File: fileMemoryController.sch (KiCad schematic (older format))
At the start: 13 parts, among them U10 74LVC1G74, U12 74AHC244, U15 74AHCT1G04, U21 74AHCT244, U22 74CBTLV16212, U40 74AHC273, U41 74AHC1G04

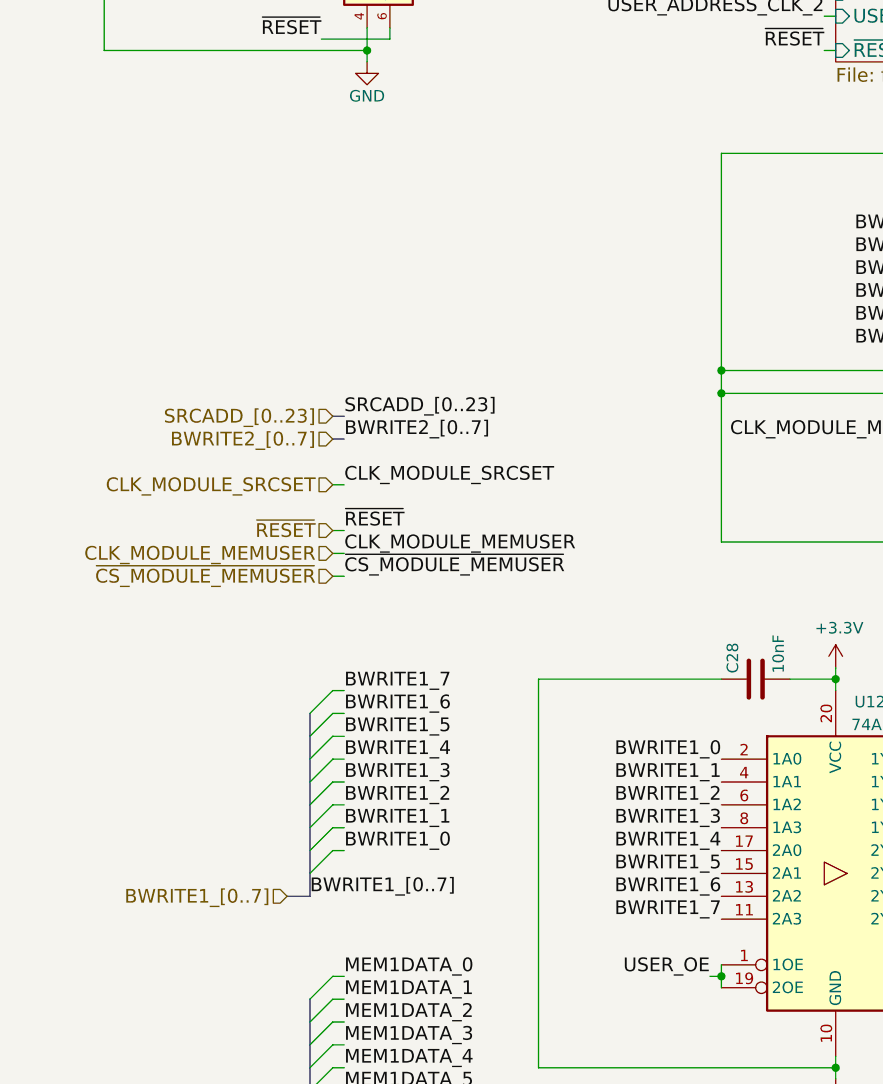
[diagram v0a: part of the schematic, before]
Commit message: V5.1 (#15)
* Remove compatibility for 5.0, 4.x and add 5.1+

* Fix switched pins on SN74LV393A #7

* Removed capacitor on 12V #11

* Add/Modify power decoupling capacitor #10

* Removing ADDSCR_CLK delay #9

* Schematics : set version 5.1, 2021 copyright and publish date

* Put non-electrolytic capacitor #10

* Set every capacitor size to 0805

* Add new footprint for J7 TE_3-641124-6 #6

* Schematic : set pinHeader on J12 #4

* Netlist, apply change to board, clean track, #6 #4 #12 #10

* Set version to 5.1, 2021 copyright and date, replace the missing QRcode

* Back the MM1 connectors #8

* Replace capacitor for U22 U23 U24 #13

* Better decoupling

* Increase version, year to 2021, clear status

* Precise the molex connector for power supply

* First step, import ses

* Clean bottom layer

* #14 Set the BWRITE2 bus instead of BWRITE1 on U12

* netlist, redo autorouting and cleaning

* use shields.io for colored badge

* Update gerbert files

* Changelog, updated BOM

* Small revision on blockDiagram

* Update README.md

* exporting pcb in pdf

* 3D images, diagram.png

* Update schematics pdf

* redo wavedrom_24bitsCounter
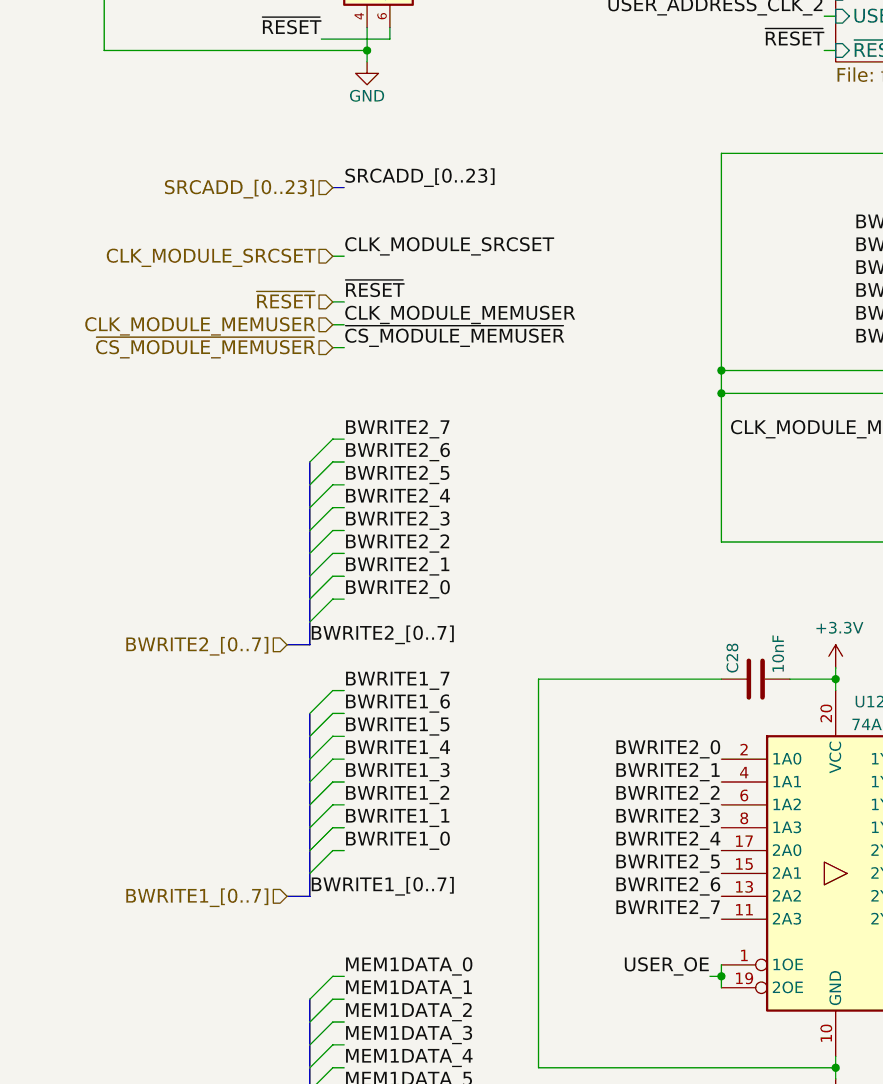
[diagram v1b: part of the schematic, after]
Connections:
- net BWRITE1_0: no longer U12.2 (1A0)
- net BWRITE1_1: no longer U12.4 (1A1)
- net BWRITE1_2: no longer U12.6 (1A2)
- net BWRITE1_3: no longer U12.8 (1A3)
- net BWRITE1_4: no longer U12.17 (2A0)
- net BWRITE1_5: no longer U12.15 (2A1)
- net BWRITE1_6: no longer U12.13 (2A2)
- net BWRITE1_7: no longer U12.11 (2A3)
- new net BWRITE2_0: U12.2 (1A0)
- new net BWRITE2_1: U12.4 (1A1)
- new net BWRITE2_2: U12.6 (1A2)
- new net BWRITE2_3: U12.8 (1A3)
- new net BWRITE2_4: U12.17 (2A0)
- new net BWRITE2_5: U12.15 (2A1)
- new net BWRITE2_6: U12.13 (2A2)
- new net BWRITE2_7: U12.11 (2A3)
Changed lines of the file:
@@
 Sheet 8 10
 Title "GCM"
-Date "2020-11-23"
-Rev "V5.0"
+Date "2021-02-16"
+Rev "V5.1"
 Comp "Guillaume Guillet"
-Comment1 "Copyright Guillaume Guillet 2020"
+Comment1 "Copyright Guillaume Guillet 2021"
 Comment2 "Licensed under CERN-OHL-W v2 or later"
 Comment3 ""
@@
 	0    -1   -1   0
 $EndComp
-Text Label 3300 4600 2    60   ~ 0
-BWRITE1_0
-Text Label 3300 4700 2    60   ~ 0
-BWRITE1_1
-Text Label 3300 4800 2    60   ~ 0
-BWRITE1_2
-Text Label 3300 4900 2    60   ~ 0
-BWRITE1_3
-Text Label 3300 5000 2    60   ~ 0
-BWRITE1_4
-Text Label 3300 5100 2    60   ~ 0
-BWRITE1_5
-Text Label 3300 5200 2    60   ~ 0
-BWRITE1_6
-Text Label 3300 5300 2    60   ~ 0
-BWRITE1_7
 Wire Wire Line
 	3800 6000 3800 5950
@@
 Text Label 1650 7400 0    60   ~ 0
 MEM2DATA_7
-Text Label 1650 3400 0    60   ~ 0
+Text Label 1650 2400 0    60   ~ 0
 CLK_MODULE_SRCSET
 Text Label 10250 1200 2    60   ~ 0
@@
 	1    0    0    -1
 $EndComp
-Text HLabel 1600 3200 0    60   Input ~ 0
-BWRITE2_[0..7]
-Text HLabel 1600 3100 0    60   Input ~ 0
+Text HLabel 1600 2100 0    60   Input ~ 0
 SRCADD_[0..23]
-Text Label 1650 3100 0    60   ~ 0
+Text Label 1650 2100 0    60   ~ 0
 SRCADD_[0..23]
-Text Label 1650 3200 0    60   ~ 0
-BWRITE2_[0..7]
-Wire Bus Line
-	1600 3100 1650 3100
-Wire Bus Line
-	1650 3200 1600 3200
+Wire Bus Line
+	1600 2100 1650 2100
 Text Label 3750 850  2    60   ~ 0
 SRCADD_[0..23]
@@
 Wire Wire Line
 	10050 6350 10100 6350
-Text HLabel 1600 3400 0    60   Input ~ 0
+Text HLabel 1600 2400 0    60   Input ~ 0
 CLK_MODULE_SRCSET
 Wire Wire Line
-	1600 3400 1650 3400
+	1600 2400 1650 2400
 Wire Wire Line
 	7850 3900 7150 3900
@@
 Text Label 4350 2800 2    60   ~ 0
 BWRITE1_5
-Text Label 1650 3700 0    60   ~ 0
+Text Label 1650 2700 0    60   ~ 0
 CLK_MODULE_MEMUSER
-Text HLabel 1600 3700 0    60   Input ~ 0
+Text HLabel 1600 2700 0    60   Input ~ 0
 CLK_MODULE_MEMUSER
 Wire Wire Line
-	1600 3700 1650 3700
-Text Label 1650 3600 0    60   ~ 0
+	1600 2700 1650 2700
+Text Label 1650 2600 0    60   ~ 0
 ~RESET
-Text HLabel 1600 3600 0    60   Input ~ 0
+Text HLabel 1600 2600 0    60   Input ~ 0
 ~RESET
 Wire Wire Line
-	1600 3600 1650 3600
+	1600 2600 1650 2600
 Text Label 1550 1450 2    60   ~ 0
 ~RESET
@@
 Text Label 5350 2500 0    60   ~ 0
 USER_~OE
-Text Label 1650 3800 0    60   ~ 0
+Text Label 1650 2800 0    60   ~ 0
 ~CS_MODULE_MEMUSER
-Text HLabel 1600 3800 0    60   Input ~ 0
+Text HLabel 1600 2800 0    60   Input ~ 0
 ~CS_MODULE_MEMUSER
 Wire Wire Line
-	1600 3800 1650 3800
+	1600 2800 1650 2800
 Text Label 7750 6000 2    60   ~ 0
 USER_~OE
@@
 	7150 3900 7150 4300
 Connection ~ 7150 3900
+Text HLabel 1400 4100 0    60   Input ~ 0
+BWRITE2_[0..7]
+Wire Bus Line
+	1500 4100 1400 4100
+Wire Wire Line
+	1650 3900 1600 3900
+Wire Wire Line
+	1650 3800 1600 3800
+Wire Wire Line
+	1650 3700 1600 3700
+Wire Wire Line
+	1650 3600 1600 3600
+Wire Wire Line
+	1650 3500 1600 3500
+Wire Wire Line
+	1650 3400 1600 3400
+Wire Wire Line
+	1650 3300 1600 3300
+Wire Wire Line
+	1650 3200 1600 3200
+Entry Wire Line
+	1600 3900 1500 4000
+Entry Wire Line
+	1600 3800 1500 3900
+Entry Wire Line
+	1600 3700 1500 3800
+Entry Wire Line
+	1600 3600 1500 3700
+Entry Wire Line
+	1600 3500 1500 3600
+Entry Wire Line
+	1600 3400 1500 3500
+Entry Wire Line
+	1600 3300 1500 3400
+Entry Wire Line
+	1600 3200 1500 3300
+Text Label 1500 4100 0    60   ~ 0
+BWRITE2_[0..7]
+Text Label 1650 3900 0    60   ~ 0
+BWRITE2_0
+Text Label 1650 3800 0    60   ~ 0
+BWRITE2_1
+Text Label 1650 3700 0    60   ~ 0
+BWRITE2_2
+Text Label 1650 3600 0    60   ~ 0
+BWRITE2_3
+Text Label 1650 3500 0    60   ~ 0
+BWRITE2_4
+Text Label 1650 3400 0    60   ~ 0
+BWRITE2_5
+Text Label 1650 3300 0    60   ~ 0
+BWRITE2_6
+Text Label 1650 3200 0    60   ~ 0
+BWRITE2_7
+Text Label 3300 4600 2    60   ~ 0
+BWRITE2_0
+Text Label 3300 4700 2    60   ~ 0
+BWRITE2_1
+Text Label 3300 4800 2    60   ~ 0
+BWRITE2_2
+Text Label 3300 4900 2    60   ~ 0
+BWRITE2_3
+Text Label 3300 5000 2    60   ~ 0
+BWRITE2_4
+Text Label 3300 5100 2    60   ~ 0
+BWRITE2_5
+Text Label 3300 5200 2    60   ~ 0
+BWRITE2_6
+Text Label 3300 5300 2    60   ~ 0
+BWRITE2_7
 Wire Bus Line
 	10000 4050 10000 4850
@@
 Wire Bus Line
 	1500 6800 1500 7600
+Wire Bus Line
+	1500 3300 1500 4100
 $EndSCHEMATC
